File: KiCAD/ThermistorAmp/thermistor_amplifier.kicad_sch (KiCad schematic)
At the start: 14 parts, among them J1 Screw_Terminal_01x02, J2 Screw_Terminal_01x03, J3 Screw_Terminal_01x02, U1 RKZE_DCDC_Conv, U2 AD623ANZ

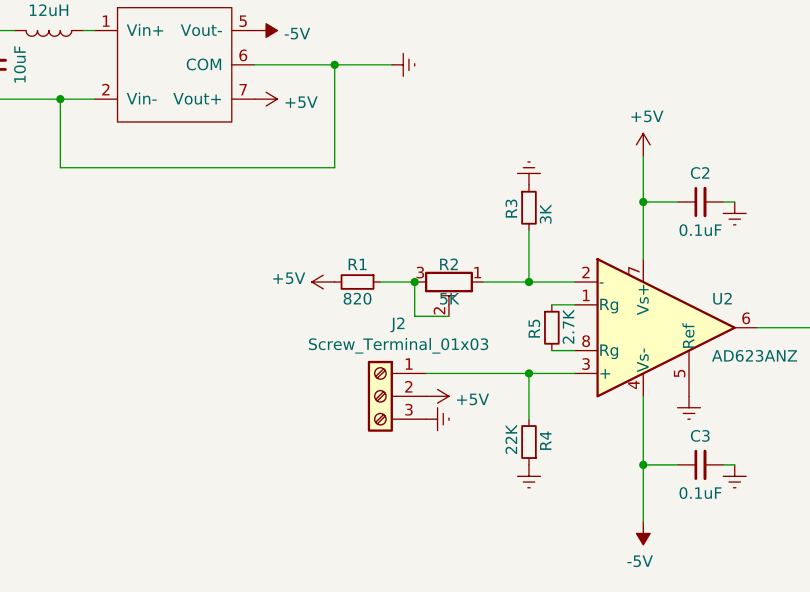
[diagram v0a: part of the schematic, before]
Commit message: Update thermistor amp to V2
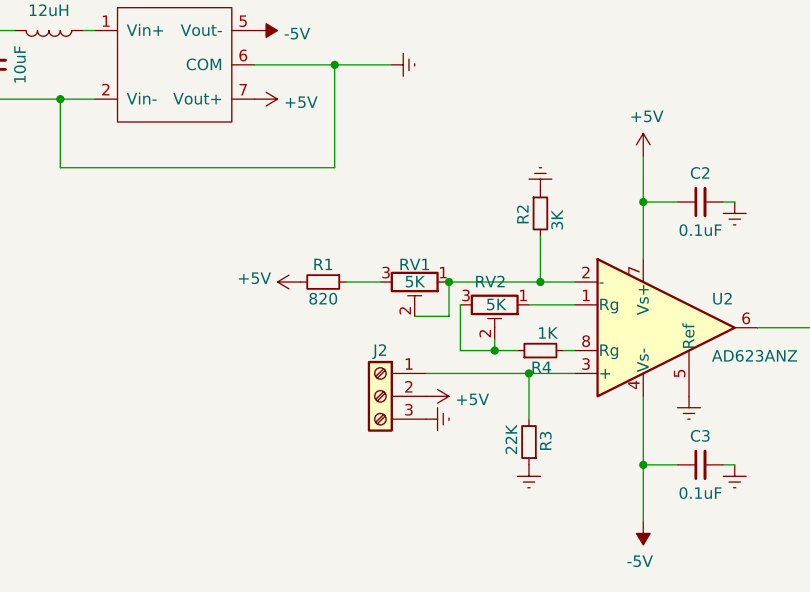
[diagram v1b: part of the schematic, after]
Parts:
- added RV2: 5K, Potentiometer_THT:Potentiometer_Bourns_3386P_Vertical, symbol Device:R_Potentiometer_Trim
- C1, C2, C3: footprint Capacitor_SMD:C_1206_3216Metric_Pad1.42x1.75mm_HandSolder -> Capacitor_THT:C_Disc_D5.0mm_W2.5mm_P2.50mm
- L1: footprint thermistor_amp:RecomInductor -> Capacitor_THT:C_Radial_D5.0mm_H7.0mm_P2.00mm
- R1: footprint Resistor_SMD:R_1206_3216Metric_Pad1.42x1.75mm_HandSolder -> Resistor_THT:R_Axial_DIN0207_L6.3mm_D2.5mm_P10.16mm_Horizontal
- R2: renamed from R3; footprint Resistor_SMD:R_1206_3216Metric_Pad1.42x1.75mm_HandSolder -> Resistor_THT:R_Axial_DIN0207_L6.3mm_D2.5mm_P10.16mm_Horizontal
- R3: renamed from R4; footprint Resistor_SMD:R_1206_3216Metric_Pad1.42x1.75mm_HandSolder -> Resistor_THT:R_Axial_DIN0207_L6.3mm_D2.5mm_P10.16mm_Horizontal
- R4: renamed from R5; value 2.7K -> 1K; footprint Resistor_SMD:R_1206_3216Metric_Pad1.42x1.75mm_HandSolder -> Resistor_THT:R_Axial_DIN0207_L6.3mm_D2.5mm_P10.16mm_Horizontal
- renumbered R2 to RV1
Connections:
- net at U2.1 (Rg): now also RV2.1; no longer R4.1
- net at R2.2, RV1.1, U2.2 (-): now also RV1.2
- net at R1.1, RV1.3: no longer RV1.2
- new net: R4.1, RV2.2, RV2.3
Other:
- moved on the sheet: R1, R2, R4, RV1
